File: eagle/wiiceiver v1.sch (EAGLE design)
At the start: 16 parts, among them IC1 ATmega328P

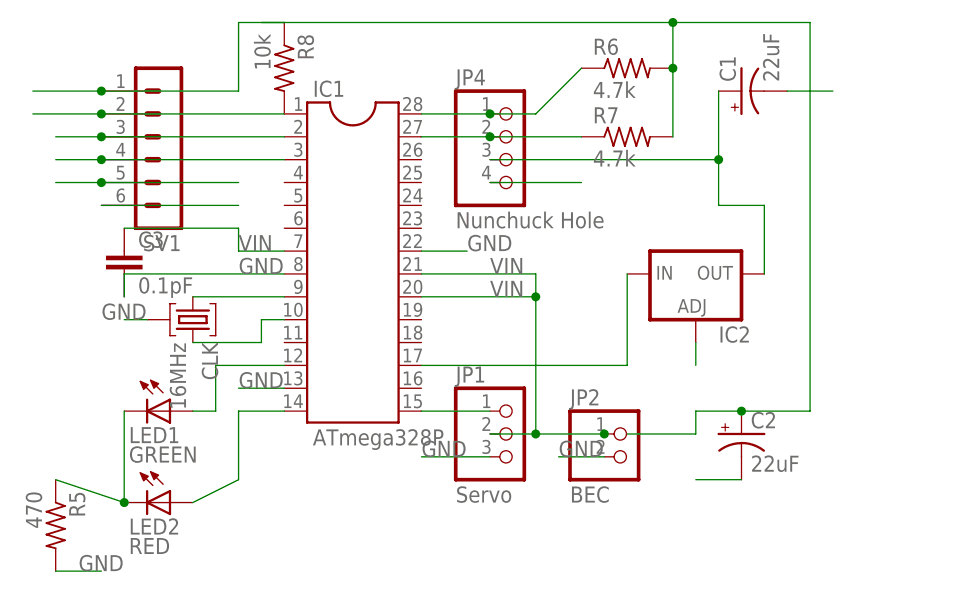
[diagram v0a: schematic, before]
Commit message: minor update for calibration function
calibrates in 1s now, and more reliably

also some minor changes to the schematic, fixing glitches
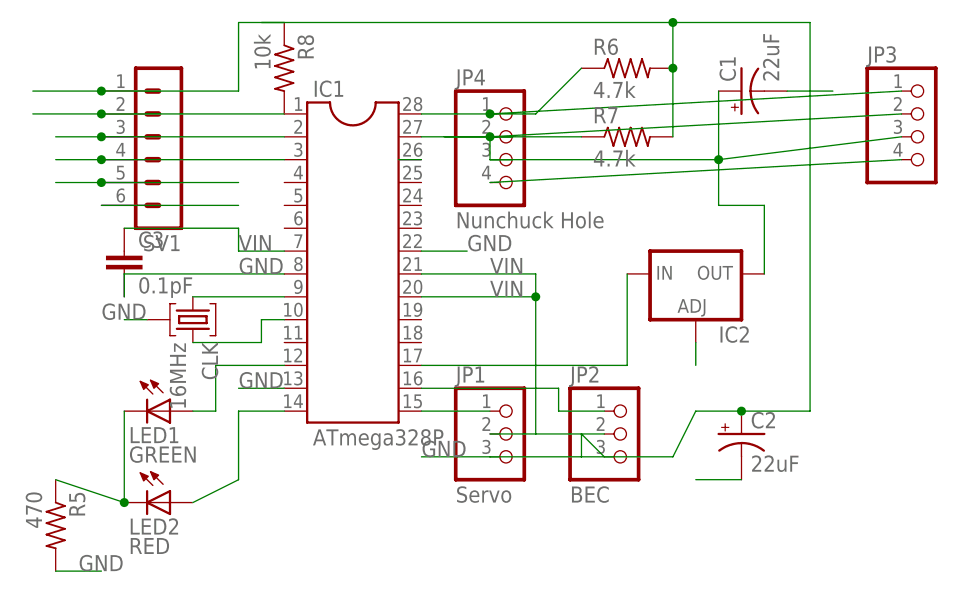
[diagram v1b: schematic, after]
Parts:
- added JP3: (no value), pinhead:PINHD-1X4
- JP2: device pinhead:PINHD-1X2 -> pinhead:PINHD-1X3
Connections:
- new net N$3: IC1.26
- new net N$4: IC1.16, JP2.1
- net GND: now also C2.+, JP2.3, JP3.4, R6.2, R7.2, R8.1, SV1.1; no longer JP2.2
- net N$16: now also JP3.2, JP3.3
- net N$21: now also JP3.1
- net VIN: now also JP2.2; no longer C2.+, JP2.1, R6.2, R7.2, R8.1, SV1.1
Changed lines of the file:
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@@
 <part name="LED2" library="led" deviceset="LED" device="3MM" value="RED"/>
 <part name="JP1" library="pinhead" deviceset="PINHD-1X3" device="" value="Servo"/>
-<part name="JP2" library="pinhead" deviceset="PINHD-1X2" device="" value="BEC"/>
+<part name="JP2" library="pinhead" deviceset="PINHD-1X3" device="" value="BEC"/>
 <part name="CLK" library="crystal" deviceset="IXF" device="A" value="16MHz"/>
 <part name="JP4" library="pinhead" deviceset="PINHD-1X4" device="" value="Nunchuck Hole"/>
@@
 <part name="IC2" library="v-reg" deviceset="LM317TS" device=""/>
 <part name="SV1" library="con-lstb" deviceset="MA06-1" device=""/>
+<part name="JP3" library="pinhead" deviceset="PINHD-1X4" device=""/>
 </parts>
 <sheets>
@@
 <instance part="LED2" gate="G$1" x="53.34" y="66.04" rot="R270"/>
 <instance part="JP1" gate="A" x="91.44" y="73.66"/>
-<instance part="JP2" gate="G$1" x="104.14" y="71.12"/>
+<instance part="JP2" gate="A" x="104.14" y="73.66"/>
 <instance part="CLK" gate="G$1" x="55.88" y="86.36" rot="R270"/>
 <instance part="JP4" gate="A" x="91.44" y="104.14"/>
@@
 <instance part="IC2" gate="1" x="111.76" y="91.44"/>
 <instance part="SV1" gate="1" x="53.34" y="104.14" rot="R180"/>
+<instance part="JP3" gate="A" x="137.16" y="106.68"/>
 </instances>
 <busses>
@@
 <wire x1="119.38" y1="91.44" x2="119.38" y2="99.06" width="0.1524" layer="91"/>
 <wire x1="119.38" y1="99.06" x2="114.3" y2="99.06" width="0.1524" layer="91"/>
+<wire x1="114.3" y1="104.14" x2="134.62" y2="106.68" width="0.1524" layer="91"/>
+<pinref part="JP3" gate="A" pin="3"/>
+<wire x1="88.9" y1="104.14" x2="88.9" y2="106.68" width="0.1524" layer="91"/>
+<pinref part="JP3" gate="A" pin="2"/>
+<wire x1="88.9" y1="106.68" x2="134.62" y2="109.22" width="0.1524" layer="91"/>
 </segment>
 </net>
@@
 <pinref part="JP4" gate="A" pin="1"/>
 <pinref part="IC1" gate="G$1" pin="28"/>
-<wire x1="88.9" y1="109.22" x2="81.28" y2="109.22" width="0.1524" layer="91"/>
 <pinref part="R6" gate="G$1" pin="1"/>
 <wire x1="93.98" y1="109.22" x2="99.06" y2="114.3" width="0.1524" layer="91"/>
 <wire x1="88.9" y1="109.22" x2="93.98" y2="109.22" width="0.1524" layer="91"/>
 <junction x="88.9" y="109.22"/>
+<wire x1="88.9" y1="109.22" x2="81.28" y2="109.22" width="0.1524" layer="91"/>
+<pinref part="JP3" gate="A" pin="1"/>
+<wire x1="88.9" y1="109.22" x2="134.62" y2="111.76" width="0.1524" layer="91"/>
+</segment>
+<segment>
+<wire x1="91.44" y1="106.68" x2="83.82" y2="106.68" width="0.1524" layer="91"/>
 </segment>
 </net>
@@
 <segment>
 <pinref part="JP4" gate="A" pin="4"/>
-<wire x1="88.9" y1="101.6" x2="99.06" y2="101.6" width="0.1524" layer="91"/>
-</segment>
-<segment>
-<pinref part="JP2" gate="G$1" pin="2"/>
-<wire x1="101.6" y1="71.12" x2="96.52" y2="71.12" width="0.1524" layer="91"/>
-<label x="96.52" y="71.12" size="1.778" layer="95"/>
-</segment>
-<segment>
-<pinref part="JP1" gate="A" pin="3"/>
-<wire x1="88.9" y1="71.12" x2="81.28" y2="71.12" width="0.1524" layer="91"/>
-<label x="81.28" y="71.12" size="1.778" layer="95"/>
+<wire x1="134.62" y1="104.14" x2="88.9" y2="101.6" width="0.1524" layer="91"/>
+<pinref part="JP3" gate="A" pin="4"/>
 </segment>
 <segment>
@@
 <wire x1="111.76" y1="83.82" x2="111.76" y2="81.28" width="0.1524" layer="91"/>
 </segment>
-</net>
-<net name="VIN" class="0">
-<segment>
-<pinref part="JP2" gate="G$1" pin="1"/>
-<pinref part="JP1" gate="A" pin="2"/>
-<wire x1="88.9" y1="73.66" x2="93.98" y2="73.66" width="0.1524" layer="91"/>
-<wire x1="93.98" y1="73.66" x2="101.6" y2="73.66" width="0.1524" layer="91"/>
-<wire x1="93.98" y1="73.66" x2="93.98" y2="88.9" width="0.1524" layer="91"/>
-<pinref part="IC1" gate="G$1" pin="21"/>
-<wire x1="93.98" y1="88.9" x2="93.98" y2="91.44" width="0.1524" layer="91"/>
-<pinref part="IC1" gate="G$1" pin="20"/>
-<wire x1="93.98" y1="91.44" x2="81.28" y2="91.44" width="0.1524" layer="91"/>
-<wire x1="81.28" y1="88.9" x2="93.98" y2="88.9" width="0.1524" layer="91"/>
-<junction x="93.98" y="73.66"/>
-<junction x="93.98" y="88.9"/>
-<junction x="101.6" y="73.66"/>
-<label x="88.9" y="91.44" size="1.778" layer="95"/>
-<label x="88.9" y="88.9" size="1.778" layer="95"/>
-</segment>
-<segment>
-<pinref part="IC1" gate="G$1" pin="7"/>
-<wire x1="66.04" y1="93.98" x2="60.96" y2="93.98" width="0.1524" layer="91"/>
-<label x="60.96" y="93.98" size="1.778" layer="95"/>
-<pinref part="C3" gate="G$1" pin="1"/>
-<wire x1="48.26" y1="96.52" x2="60.96" y2="96.52" width="0.1524" layer="91"/>
-<wire x1="60.96" y1="96.52" x2="60.96" y2="93.98" width="0.1524" layer="91"/>
-</segment>
-<segment>
-<wire x1="104.14" y1="73.66" x2="111.76" y2="73.66" width="0.1524" layer="91"/>
-<wire x1="111.76" y1="73.66" x2="111.76" y2="76.2" width="0.1524" layer="91"/>
+<segment>
+<wire x1="109.22" y1="71.12" x2="111.76" y2="76.2" width="0.1524" layer="91"/>
 <pinref part="C2" gate="G$1" pin="+"/>
 <wire x1="111.76" y1="76.2" x2="116.84" y2="76.2" width="0.1524" layer="91"/>
@@
 <pinref part="SV1" gate="1" pin="1"/>
 <junction x="45.72" y="111.76"/>
+<pinref part="JP1" gate="A" pin="3"/>
+<label x="81.28" y="71.12" size="1.778" layer="95"/>
+<wire x1="88.9" y1="71.12" x2="81.28" y2="71.12" width="0.1524" layer="91"/>
+<wire x1="88.9" y1="71.12" x2="99.06" y2="71.12" width="0.1524" layer="91"/>
+<wire x1="99.06" y1="71.12" x2="109.22" y2="71.12" width="0.1524" layer="91"/>
+<wire x1="101.6" y1="71.12" x2="99.06" y2="73.66" width="0.1524" layer="91"/>
+<wire x1="99.06" y1="73.66" x2="99.06" y2="71.12" width="0.1524" layer="91"/>
+<pinref part="JP2" gate="A" pin="3"/>
+</segment>
+<segment>
+<wire x1="88.9" y1="104.14" x2="91.44" y2="104.14" width="0.1524" layer="91"/>
+</segment>
+</net>
+<net name="VIN" class="0">
+<segment>
+<pinref part="JP1" gate="A" pin="2"/>
+<wire x1="88.9" y1="73.66" x2="93.98" y2="73.66" width="0.1524" layer="91"/>
+<wire x1="93.98" y1="73.66" x2="93.98" y2="88.9" width="0.1524" layer="91"/>
+<pinref part="IC1" gate="G$1" pin="21"/>
+<wire x1="93.98" y1="88.9" x2="93.98" y2="91.44" width="0.1524" layer="91"/>
+<pinref part="IC1" gate="G$1" pin="20"/>
+<wire x1="93.98" y1="91.44" x2="81.28" y2="91.44" width="0.1524" layer="91"/>
+<wire x1="81.28" y1="88.9" x2="93.98" y2="88.9" width="0.1524" layer="91"/>
+<junction x="93.98" y="88.9"/>
+<label x="88.9" y="91.44" size="1.778" layer="95"/>
+<label x="88.9" y="88.9" size="1.778" layer="95"/>
+<pinref part="JP2" gate="A" pin="2"/>
+<wire x1="101.6" y1="73.66" x2="93.98" y2="73.66" width="0.1524" layer="91"/>
+</segment>
+<segment>
+<pinref part="IC1" gate="G$1" pin="7"/>
+<wire x1="66.04" y1="93.98" x2="60.96" y2="93.98" width="0.1524" layer="91"/>
+<label x="60.96" y="93.98" size="1.778" layer="95"/>
+<pinref part="C3" gate="G$1" pin="1"/>
+<wire x1="48.26" y1="96.52" x2="60.96" y2="96.52" width="0.1524" layer="91"/>
+<wire x1="60.96" y1="96.52" x2="60.96" y2="93.98" width="0.1524" layer="91"/>
 </segment>
 </net>
@@
 </segment>
 </net>
+<net name="N$3" class="0">
+<segment>
+<pinref part="IC1" gate="G$1" pin="26"/>
+<wire x1="81.28" y1="104.14" x2="78.74" y2="104.14" width="0.1524" layer="91"/>
+</segment>
+</net>
+<net name="N$4" class="0">
+<segment>
+<pinref part="JP2" gate="A" pin="1"/>
+<wire x1="101.6" y1="76.2" x2="96.52" y2="76.2" width="0.1524" layer="91"/>
+<wire x1="96.52" y1="76.2" x2="96.52" y2="78.74" width="0.1524" layer="91"/>
+<pinref part="IC1" gate="G$1" pin="16"/>
+<wire x1="96.52" y1="78.74" x2="81.28" y2="78.74" width="0.1524" layer="91"/>
+</segment>
+</net>
